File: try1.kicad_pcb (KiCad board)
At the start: 2 copper layers, 175.3 x 119.4 mm, 33 parts, among them J10 Archon-connector-modules-Driv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, J11 Archon-connector-modules-Driv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, J2 Archon-connector-modules-Heat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, J21 DB37, J22 DB37, J3 Archon-connector-modules-Driv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, J31 DB9, J4 Archon-connector-modules-LVBi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, J41 CONN_DVI, J5 Archon-connector-modules-ADC, J6 Archon-connector-modules-ADC, J7 Archon-connector-modules-ADC, J8 Archon-connector-modules-ADC, J9 Archon-connector-modules-HVBi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, P1 CONN_02X02

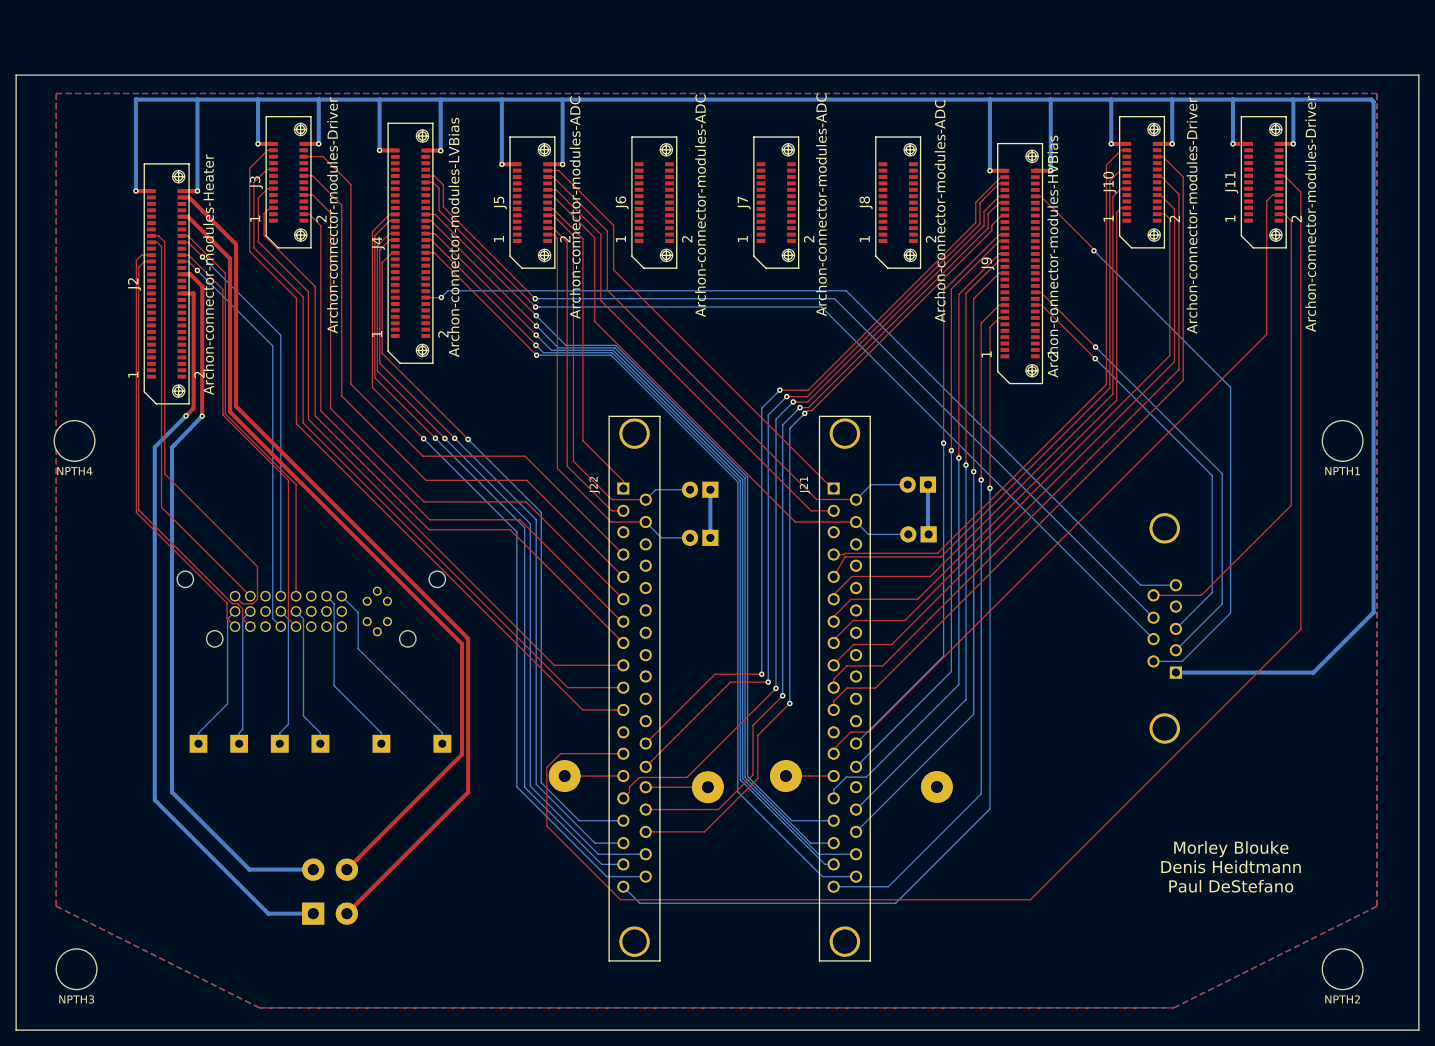
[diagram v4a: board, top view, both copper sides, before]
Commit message: Add Hard GND Traces From Jumpers
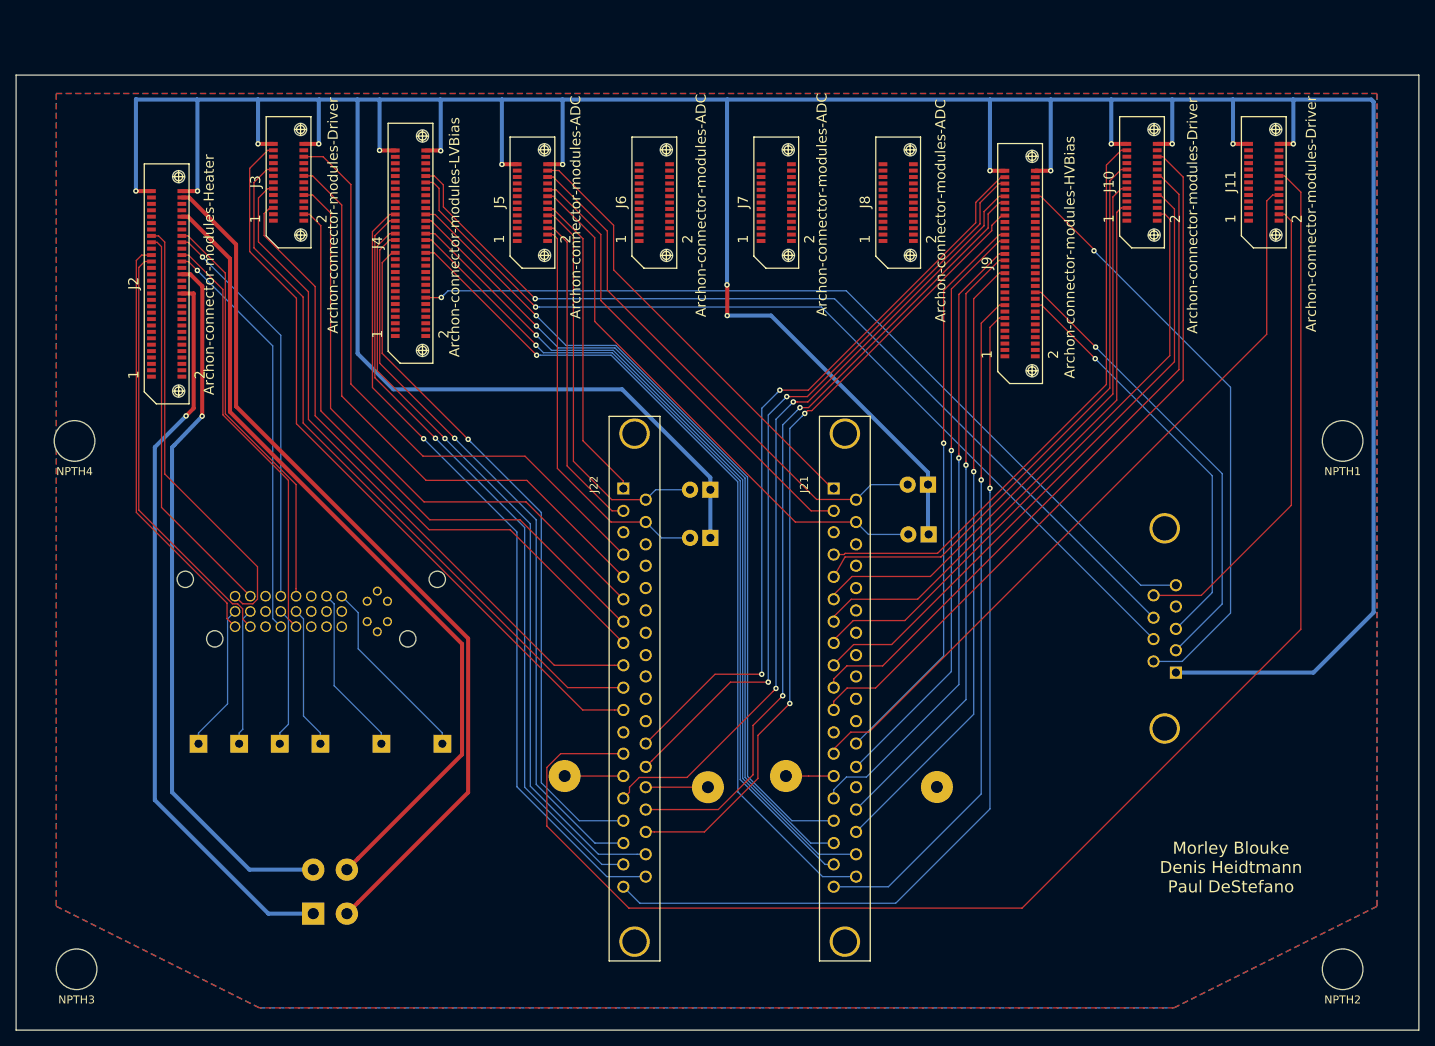
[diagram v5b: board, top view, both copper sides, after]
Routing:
- net /GND: track 389.0 -> 534.5 mm, vias 14 -> 16
- net /~ResetLog_L: track 188.3 -> 189.2 mm
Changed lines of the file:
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@@
     (links 112)
     (no_connects 2)
-    (area 41.951046 18.373109 222.731954 142.492701)
+    (area 45.767299 23.087299 221.132701 142.492701)
     (thickness 1.6)
     (drawings 10)
-    (tracks 685)
+    (tracks 702)
     (zones 0)
     (modules 33)
@@
       (drillshape 0)
       (scaleselection 1)
-      (outputdirectory C:/Users/des3/Desktop/))
+      (outputdirectory ""))
   )
   (net 0 "")
@@
       (effects (font (size 1.27 1.27) (thickness 0.1016)))
     )
-    (fp_text value Archon-connector-modules-HVBias (at 0.90932 4.16306 90) (layer F.SilkS)
+    (fp_text value Archon-connector-modules-HVBias (at 0.7876 6.2152 90) (layer F.SilkS)
       (effects (font (size 1.27 1.27) (thickness 0.1016)))
     )
@@
   (target plus (at 52.07 99.06) (size 5) (width 0.15) (layer Edge.Cuts))
   (target plus (at 52.07 35.56) (size 5) (width 0.15) (layer Edge.Cuts))
+  (segment (start 132.5626 74.93) (end 132.5626 73.406) (width 0.508) (layer B.Cu) (net 23))
+  (segment (start 88.4682 26.1874) (end 88.4428 26.162) (width 0.508) (layer B.Cu) (net 23))
+  (segment (start 132.5626 73.406) (end 121.539 62.3824) (width 0.508) (layer B.Cu) (net 23))
+  (segment (start 121.539 62.3824) (end 92.9386 62.3824) (width 0.508) (layer B.Cu) (net 23))
+  (segment (start 92.9386 62.3824) (end 88.4682 57.912) (width 0.508) (layer B.Cu) (net 23))
+  (segment (start 88.4682 57.912) (end 88.4682 26.1874) (width 0.508) (layer B.Cu) (net 23))
+  (segment (start 83.6676 26.162) (end 88.4428 26.162) (width 0.508) (layer B.Cu) (net 23))
+  (segment (start 88.4428 26.162) (end 91.2114 26.162) (width 0.508) (layer B.Cu) (net 23))
+  (segment (start 134.6454 49.3268) (end 134.6454 26.2128) (width 0.508) (layer B.Cu) (net 23))
+  (segment (start 134.6454 26.2128) (end 134.6962 26.162) (width 0.508) (layer B.Cu) (net 23))
+  (segment (start 114.0714 26.162) (end 134.6962 26.162) (width 0.508) (layer B.Cu) (net 23))
+  (segment (start 134.6962 26.162) (end 167.513 26.162) (width 0.508) (layer B.Cu) (net 23))
+  (segment (start 134.6708 53.1622) (end 134.6708 49.3522) (width 0.508) (layer F.Cu) (net 23))
+  (segment (start 134.6708 49.3522) (end 134.6454 49.3268) (width 0.508) (layer F.Cu) (net 23))
+  (via (at 134.6454 49.3268) (size 0.6858) (drill 0.3302) (layers F.Cu B.Cu) (net 23))
+  (segment (start 159.766 74.295) (end 159.766 72.771) (width 0.508) (layer B.Cu) (net 23))
+  (segment (start 159.766 72.771) (end 140.1572 53.1622) (width 0.508) (layer B.Cu) (net 23))
+  (segment (start 140.1572 53.1622) (end 134.6708 53.1622) (width 0.508) (layer B.Cu) (net 23))
+  (via (at 134.6708 53.1622) (size 0.6858) (drill 0.3302) (layers F.Cu B.Cu) (net 23))
   (segment (start 205.4098 26.162) (end 215.1888 26.162) (width 0.508) (layer B.Cu) (net 23))
   (segment (start 215.1888 26.162) (end 215.4682 26.4414) (width 0.508) (layer B.Cu) (net 23))
@@
   (via (at 68.453 37.592) (size 0.6858) (drill 0.3302) (layers F.Cu B.Cu) (net 23))
   (segment (start 75.9968 26.162) (end 83.6676 26.162) (width 0.508) (layer B.Cu) (net 23))
-  (segment (start 83.6676 26.162) (end 91.2114 26.162) (width 0.508) (layer B.Cu) (net 23))
   (segment (start 83.6168 31.6992) (end 83.6168 26.2128) (width 0.508) (layer B.Cu) (net 23))
   (segment (start 83.6168 26.2128) (end 83.6676 26.162) (width 0.508) (layer B.Cu) (net 23))
@@
   (segment (start 106.52486 34.24194) (end 106.5022 34.2646) (width 0.508) (layer F.Cu) (net 23))
   (via (at 106.5022 34.2646) (size 0.6858) (drill 0.3302) (layers F.Cu B.Cu) (net 23))
-  (segment (start 114.0714 26.162) (end 167.513 26.162) (width 0.508) (layer B.Cu) (net 23))
   (segment (start 114.0968 34.2646) (end 114.0968 26.1874) (width 0.508) (layer B.Cu) (net 23))
   (segment (start 114.0968 26.1874) (end 114.0714 26.162) (width 0.508) (layer B.Cu) (net 23))
@@
   (segment (start 121.6901 107.9246) (end 113.8461 107.9246) (width 0.1524) (layer F.Cu) (net 321))
   (segment (start 113.8461 107.9246) (end 112.121949 109.648751) (width 0.1524) (layer F.Cu) (net 321))
+  (segment (start 112.121949 116.973349) (end 122.3772 127.2286) (width 0.1524) (layer F.Cu) (net 321))
   (segment (start 112.121949 109.648751) (end 112.121949 116.973349) (width 0.1524) (layer F.Cu) (net 321))
+  (segment (start 122.3772 127.2286) (end 171.5262 127.2286) (width 0.1524) (layer F.Cu) (net 321))
+  (segment (start 171.5262 127.2286) (end 206.375 92.3798) (width 0.1524) (layer F.Cu) (net 321))
   (segment (start 206.375 92.3798) (end 206.375 37.73521) (width 0.1524) (layer F.Cu) (net 321))
   (segment (start 206.375 37.73521) (end 204.34223 35.70244) (width 0.1524) (layer F.Cu) (net 321))
-  (segment (start 112.121949 116.973349) (end 121.3358 126.1872) (width 0.1524) (layer F.Cu) (net 321))
-  (segment (start 121.3358 126.1872) (end 172.5676 126.1872) (width 0.1524) (layer F.Cu) (net 321))
-  (segment (start 172.5676 126.1872) (end 206.375 92.3798) (width 0.1524) (layer F.Cu) (net 321))
   (segment (start 204.34223 35.70244) (end 203.63992 35.70244) (width 0.1524) (layer F.Cu) (net 321))
   (segment (start 203.63992 35.70244) (end 204.050132 35.70244) (width 0.1524) (layer F.Cu) (net 321))

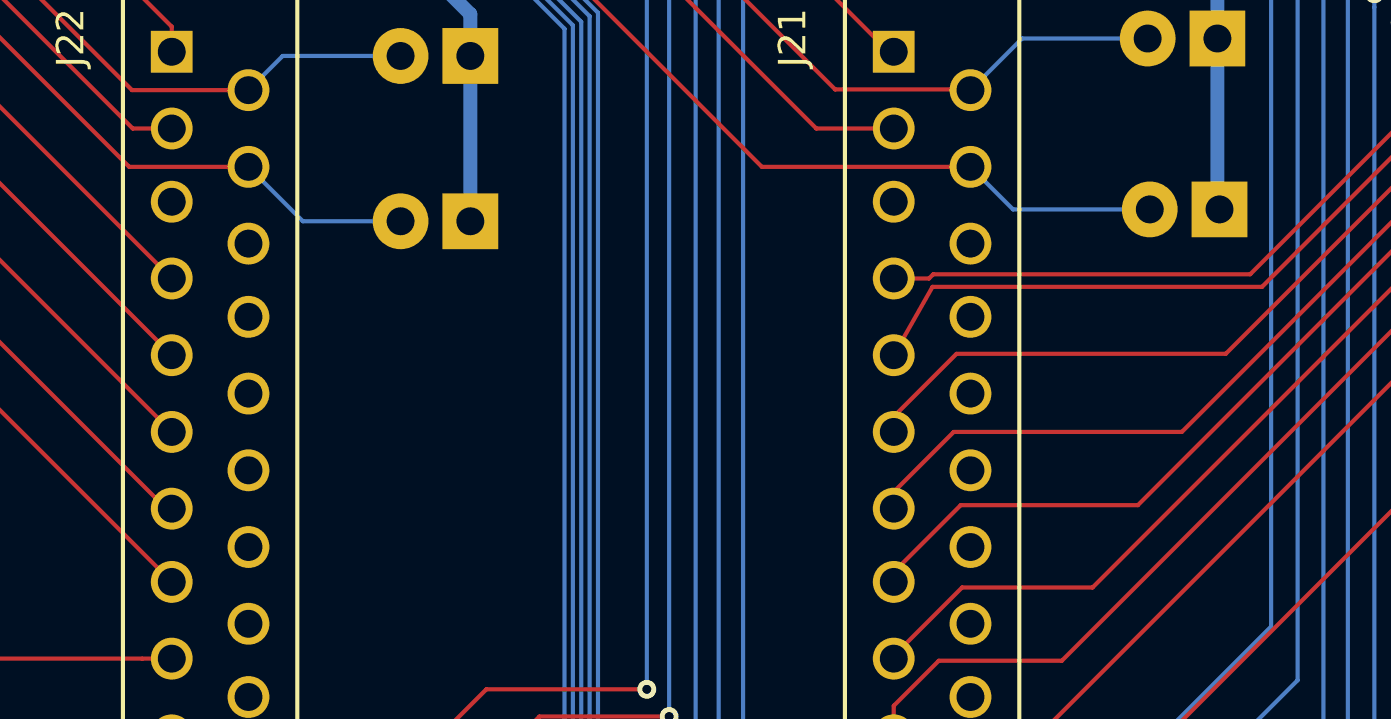
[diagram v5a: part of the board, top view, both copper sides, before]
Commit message: More Hard GND Traces
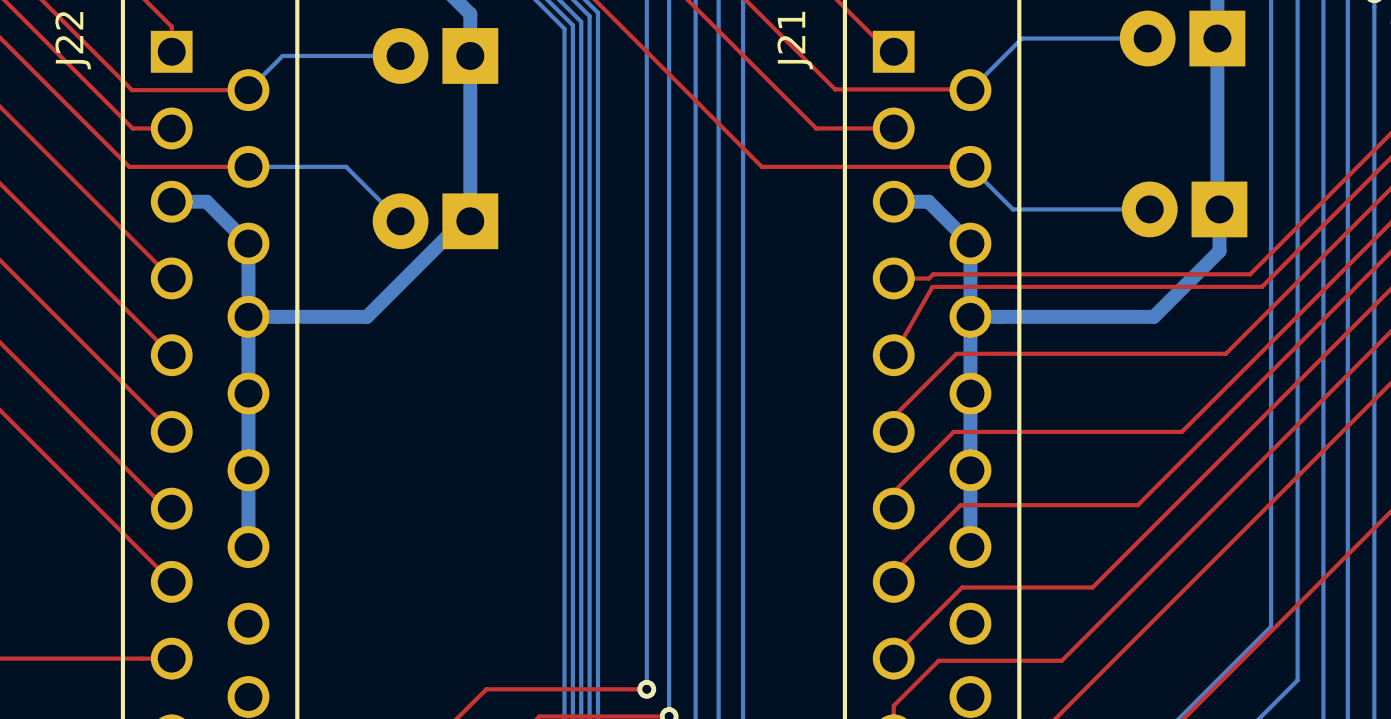
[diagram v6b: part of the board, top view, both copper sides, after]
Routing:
- net /GND: track 534.5 -> 585.0 mm
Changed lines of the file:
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@@
     (thickness 1.6)
     (drawings 10)
-    (tracks 702)
+    (tracks 723)
     (zones 0)
     (modules 33)
@@
   (target plus (at 52.07 99.06) (size 5) (width 0.15) (layer Edge.Cuts))
   (target plus (at 52.07 35.56) (size 5) (width 0.15) (layer Edge.Cuts))
+  (segment (start 150.7744 90.0176) (end 150.7744 92.8116) (width 0.508) (layer B.Cu) (net 23))
+  (segment (start 150.7744 87.2236) (end 150.7744 90.0176) (width 0.508) (layer B.Cu) (net 23))
+  (segment (start 150.7744 84.4296) (end 150.7744 87.2236) (width 0.508) (layer B.Cu) (net 23))
+  (segment (start 150.7744 81.7626) (end 150.7744 84.4296) (width 0.508) (layer B.Cu) (net 23))
+  (segment (start 159.8422 80.518) (end 159.8422 82.042) (width 0.508) (layer B.Cu) (net 23))
+  (segment (start 159.8422 82.042) (end 157.4546 84.4296) (width 0.508) (layer B.Cu) (net 23))
+  (segment (start 157.4546 84.4296) (end 151.85203 84.4296) (width 0.508) (layer B.Cu) (net 23))
+  (segment (start 151.85203 84.4296) (end 150.7744 84.4296) (width 0.508) (layer B.Cu) (net 23))
+  (segment (start 147.9804 80.2386) (end 149.2504 80.2386) (width 0.508) (layer B.Cu) (net 23))
+  (segment (start 149.2504 80.2386) (end 150.7744 81.7626) (width 0.508) (layer B.Cu) (net 23))
+  (segment (start 121.6901 80.2386) (end 122.9601 80.2386) (width 0.508) (layer B.Cu) (net 23))
+  (segment (start 122.9601 80.2386) (end 124.4841 81.7626) (width 0.508) (layer B.Cu) (net 23))
+  (segment (start 132.5626 80.9498) (end 132.562599 80.665323) (width 0.508) (layer B.Cu) (net 23))
+  (segment (start 132.562599 80.665323) (end 128.798322 84.4296) (width 0.508) (layer B.Cu) (net 23))
+  (segment (start 128.798322 84.4296) (end 125.56173 84.4296) (width 0.508) (layer B.Cu) (net 23))
+  (segment (start 125.56173 84.4296) (end 124.4841 84.4296) (width 0.508) (layer B.Cu) (net 23))
+  (segment (start 124.4841 90.0176) (end 124.4841 92.8116) (width 0.508) (layer B.Cu) (net 23))
+  (segment (start 124.4841 90.0176) (end 124.4841 87.2236) (width 0.508) (layer B.Cu) (net 23))
+  (segment (start 124.4841 84.4296) (end 124.4841 87.2236) (width 0.508) (layer B.Cu) (net 23))
+  (segment (start 124.4841 81.7626) (end 124.4841 84.4296) (width 0.508) (layer B.Cu) (net 23))
   (segment (start 132.5626 74.93) (end 132.5626 73.406) (width 0.508) (layer B.Cu) (net 23))
   (segment (start 88.4682 26.1874) (end 88.4428 26.162) (width 0.508) (layer B.Cu) (net 23))
@@
   (segment (start 118.872 51.2826) (end 145.161 77.5716) (width 0.1524) (layer F.Cu) (net 107))
   (segment (start 145.161 77.5716) (end 147.9804 77.5716) (width 0.1524) (layer F.Cu) (net 107) (status 20))
+  (segment (start 125.56173 78.9686) (end 124.4841 78.9686) (width 0.1524) (layer B.Cu) (net 111))
+  (segment (start 130.0226 80.9498) (end 128.0414 78.9686) (width 0.1524) (layer B.Cu) (net 111))
+  (segment (start 128.0414 78.9686) (end 125.56173 78.9686) (width 0.1524) (layer B.Cu) (net 111))
   (segment (start 112.21992 43.03796) (end 112.92223 43.03796) (width 0.1524) (layer F.Cu) (net 111) (status 10))
   (segment (start 113.4364 72.263) (end 120.142 78.9686) (width 0.1524) (layer F.Cu) (net 111))
@@
   (segment (start 112.92223 43.03796) (end 113.4364 43.55213) (width 0.1524) (layer F.Cu) (net 111))
   (segment (start 113.4364 43.55213) (end 113.4364 72.263) (width 0.1524) (layer F.Cu) (net 111))
-  (segment (start 126.4653 80.9498) (end 124.4841 78.9686) (width 0.1524) (layer B.Cu) (net 111) (status 20))
-  (segment (start 130.0226 80.9498) (end 126.4653 80.9498) (width 0.1524) (layer B.Cu) (net 111) (status 10))
   (segment (start 112.21992 42.23786) (end 112.92223 42.23786) (width 0.1524) (layer F.Cu) (net 113) (status 10))
   (segment (start 112.92223 42.23786) (end 114.6556 43.97123) (width 0.1524) (layer F.Cu) (net 113))
